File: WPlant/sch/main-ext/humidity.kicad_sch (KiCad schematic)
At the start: 20 parts, among them J11 HSensor, J12 HSensor, J13 HSensor, J14 HSensor, J15 HSensor, J16 HSensor, J17 HSensor, J18 WaterLevel, U12 CD74HCT4051M96, U13 CD74HCT4051M96, U14 SN74LVC1G14DBV

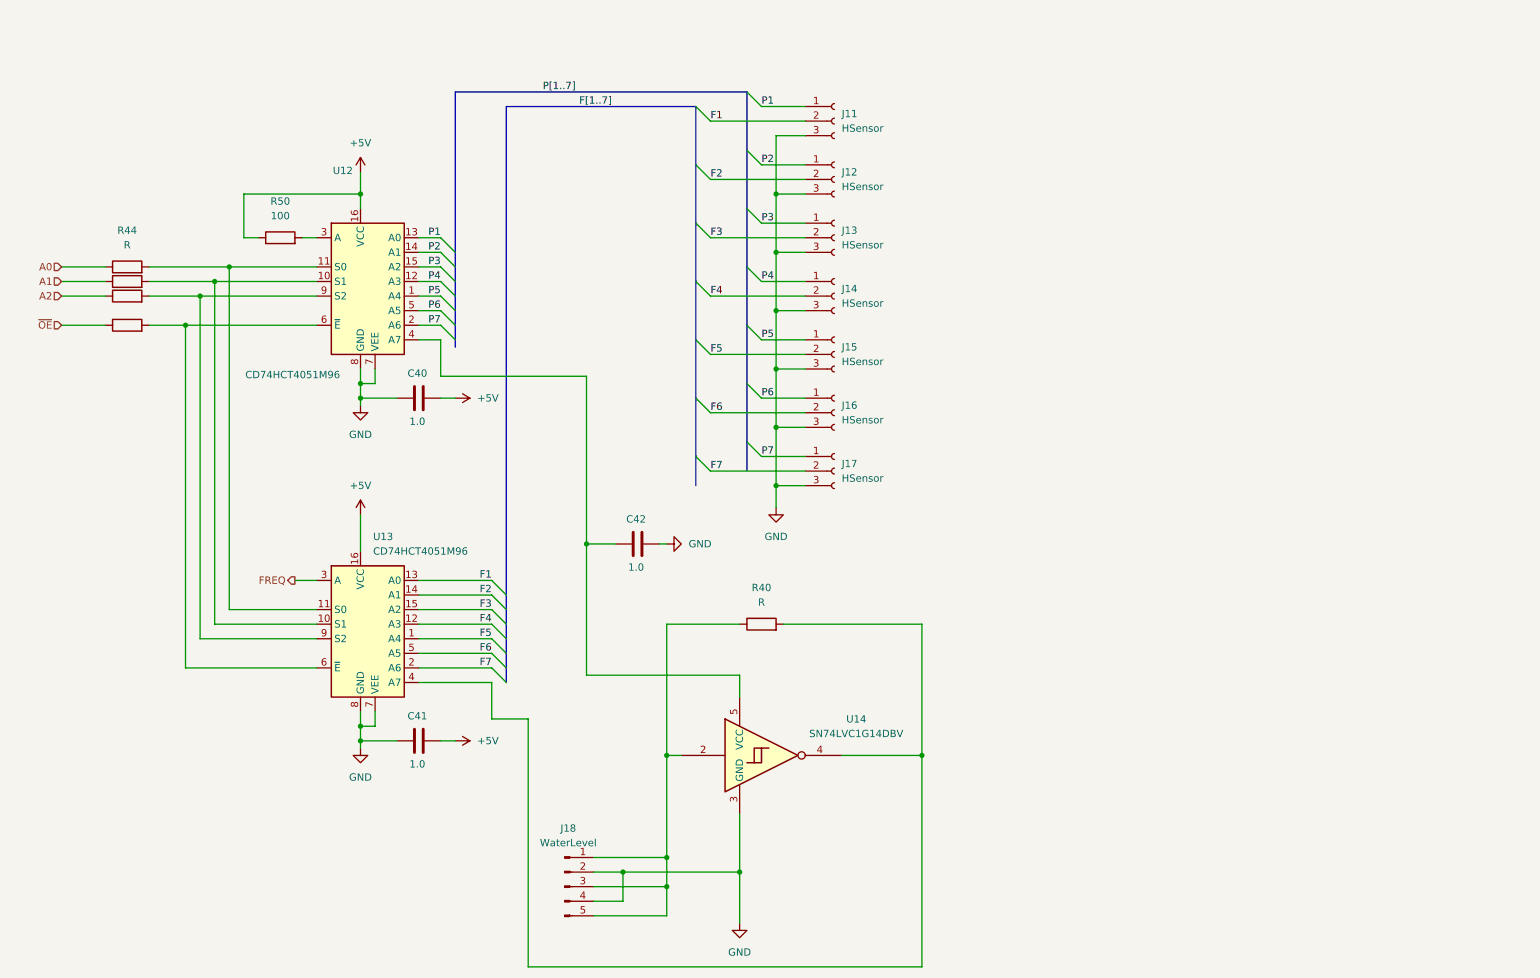
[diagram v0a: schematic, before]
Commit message: Route of WP project done
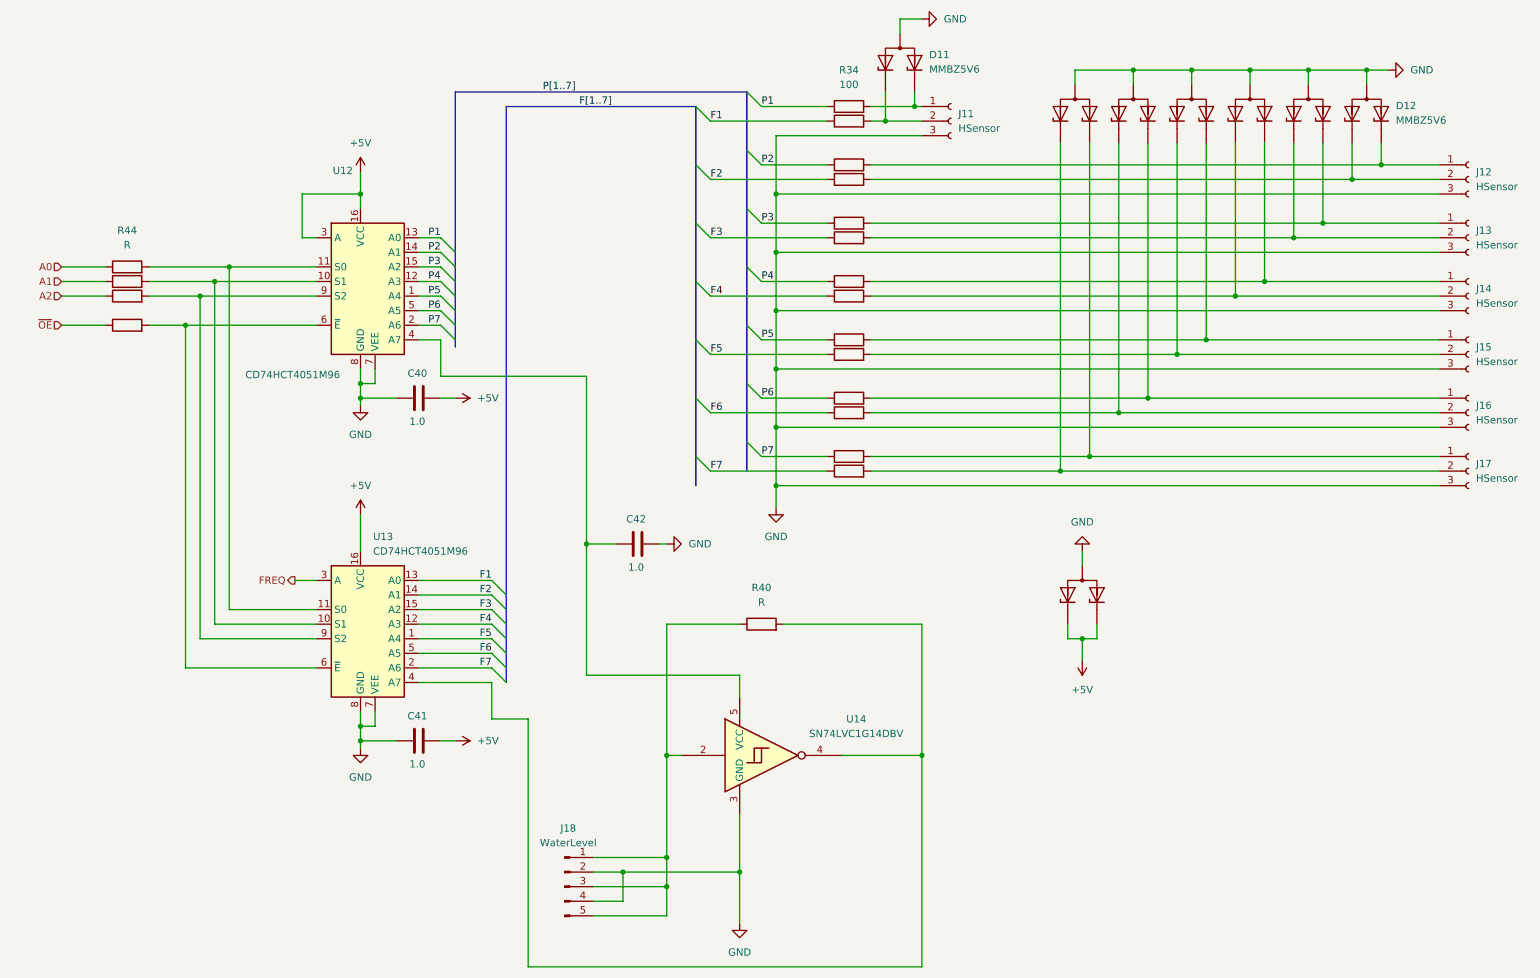
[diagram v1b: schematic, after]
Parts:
- added D11, D12, D13, D14, D15, D16, D17, D18: MMBZ5V6, Package_TO_SOT_SMD:SOT-23, symbol Diode:MMBZxx
- added R34, R51, R52, R53, R54, R55, R56, R57, R58, R59, R60, R61, R62: 100, Resistor_SMD:R_0603_1608Metric_Pad0.98x0.95mm_HandSolder, symbol Device:R
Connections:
- net +5V: now also U12.3 (A), D18.1 (K), D18.2 (K); no longer R50.1
- net F1: now also R50.1; no longer J11.2 (Pin_2)
- net F2: now also R52.1; no longer J12.2 (Pin_2)
- net F3: now also R54.1; no longer J13.2 (Pin_2)
- net F4: now also R56.1; no longer J14.2 (Pin_2)
- net F5: now also R58.1; no longer J15.2 (Pin_2)
- net F6: now also R60.1; no longer J16.2 (Pin_2)
- net F7: now also R62.1; no longer J17.2 (Pin_2)
- net GND: now also D11.3 (A), D12.3 (A), D13.3 (A), D14.3 (A), D15.3 (A), D16.3 (A), D17.3 (A), D18.3 (A)
- net P1: now also R34.1; no longer J11.1 (Pin_1)
- net P2: now also R51.1; no longer J12.1 (Pin_1)
- net P3: now also R53.1; no longer J13.1 (Pin_1)
- net P4: now also R55.1; no longer J14.1 (Pin_1)
- net P5: now also R57.1; no longer J15.1 (Pin_1)
- net P6: now also R59.1; no longer J16.1 (Pin_1)
- net P7: now also R61.1; no longer J17.1 (Pin_1)
- net at R50.2: now also J11.2 (Pin_2), D11.2 (K); no longer U12.3 (A)
- new net: D11.1 (K), J11.1 (Pin_1), R34.2
- new net: D13.1 (K), J13.1 (Pin_1), R53.2
- new net: D13.2 (K), J13.2 (Pin_2), R54.2
- new net: D12.1 (K), J12.1 (Pin_1), R51.2
- new net: D12.2 (K), J12.2 (Pin_2), R52.2
- new net: D16.1 (K), J16.1 (Pin_1), R59.2
- new net: D16.2 (K), J16.2 (Pin_2), R60.2
- new net: D14.1 (K), J14.1 (Pin_1), R55.2
- new net: D14.2 (K), J14.2 (Pin_2), R56.2
- new net: D17.1 (K), J17.1 (Pin_1), R61.2
- new net: D17.2 (K), J17.2 (Pin_2), R62.2
- new net: D15.1 (K), J15.1 (Pin_1), R57.2
- new net: D15.2 (K), J15.2 (Pin_2), R58.2
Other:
- moved on the sheet: J11, J12, J13, J14, J15, J16, J17

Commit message: Upate values in SCH of WP
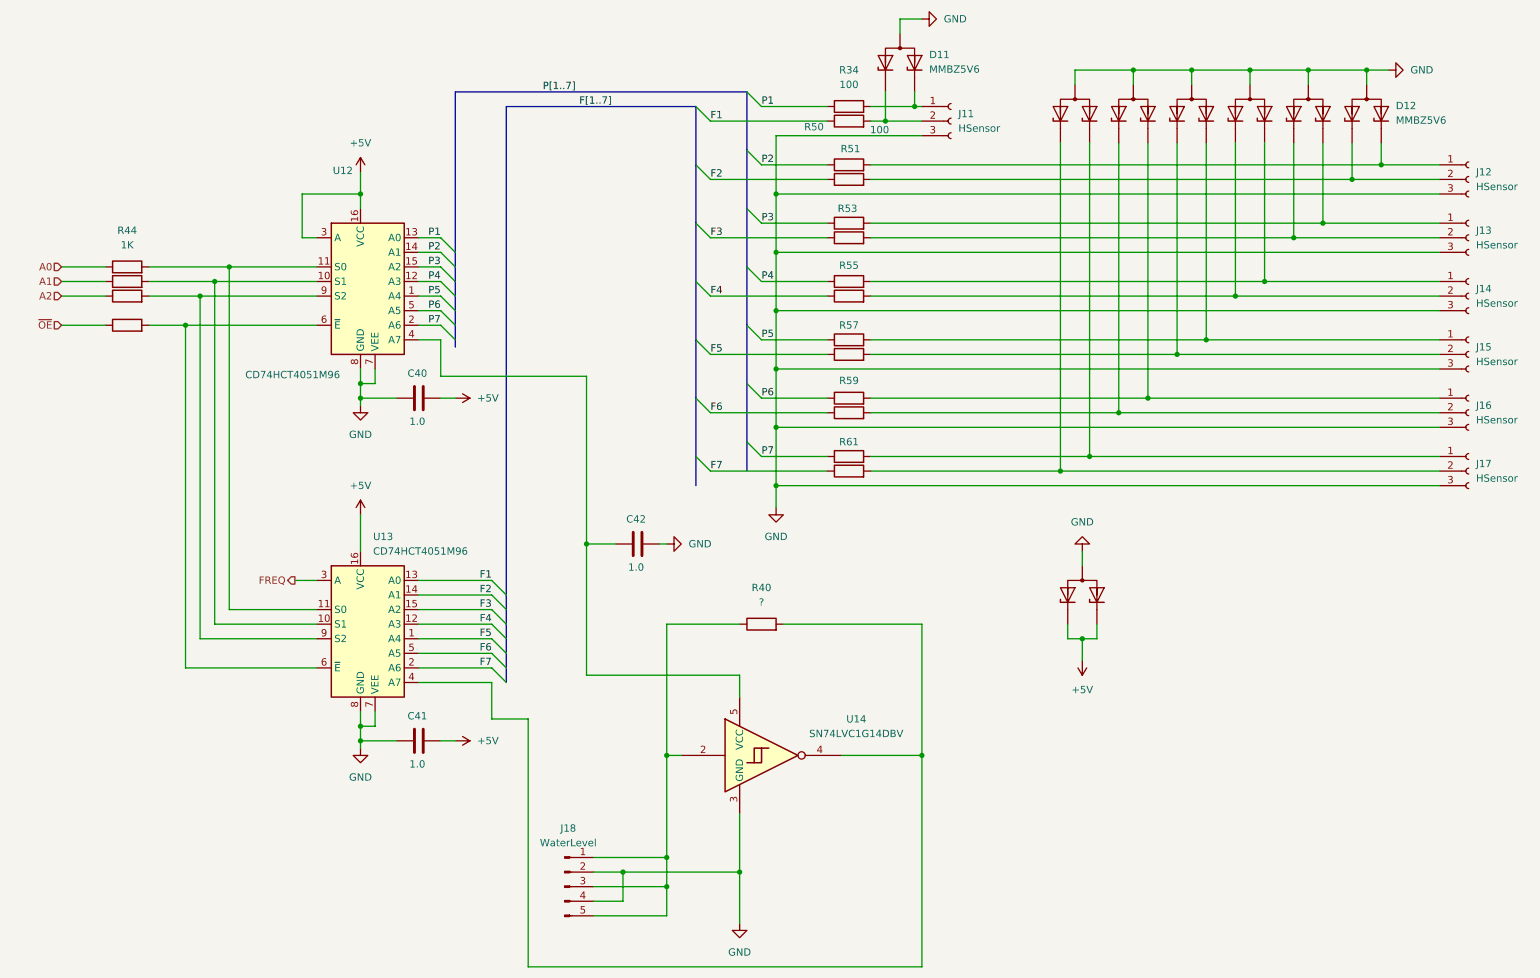
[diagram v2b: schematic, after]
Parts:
- R40: value R -> ?
- R44, R45, R46, R47: value R -> 1K
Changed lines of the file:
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@@
 		(on_board yes)
 		(dnp no)
-		(fields_autoplaced yes)
 		(property "Reference" "R50"
-			(at 162.56 27.94 90)
-			(effects
-				(font
-					(size 1.27 1.27)
-				)
-				(hide yes)
+			(at 156.464 35.306 90)
+			(effects
+				(font
+					(size 1.27 1.27)
+				)
 			)
 		)
 		(property "Value" "100"
-			(at 162.56 30.48 90)
-			(effects
-				(font
-					(size 1.27 1.27)
-				)
-				(hide yes)
+			(at 167.894 35.814 90)
+			(effects
+				(font
+					(size 1.27 1.27)
+				)
 			)
 		)
@@
 			)
 		)
-		(property "Value" "R"
+		(property "Value" "1K"
 			(at 36.83 60.96 90)
 			(effects
@@
 			)
 		)
-		(property "Value" "R"
+		(property "Value" "?"
 			(at 147.32 118.11 90)
 			(effects
@@
 		(on_board yes)
 		(dnp no)
-		(fields_autoplaced yes)
 		(property "Reference" "R53"
-			(at 162.56 45.72 90)
-			(effects
-				(font
-					(size 1.27 1.27)
-				)
-				(hide yes)
+			(at 162.306 49.53 90)
+			(effects
+				(font
+					(size 1.27 1.27)
+				)
 			)
 		)
@@
 			)
 		)
-		(property "Value" "R"
+		(property "Value" "1K"
 			(at 36.83 58.42 90)
 			(effects
@@
 		(on_board yes)
 		(dnp no)
-		(fields_autoplaced yes)
 		(property "Reference" "R55"
-			(at 162.56 55.88 90)
-			(effects
-				(font
-					(size 1.27 1.27)
-				)
-				(hide yes)
+			(at 162.56 59.436 90)
+			(effects
+				(font
+					(size 1.27 1.27)
+				)
 			)
 		)
@@
 		(on_board yes)
 		(dnp no)
-		(fields_autoplaced yes)
 		(property "Reference" "R61"
-			(at 162.56 86.36 90)
-			(effects
-				(font
-					(size 1.27 1.27)
-				)
-				(hide yes)
+			(at 162.56 90.17 90)
+			(effects
+				(font
+					(size 1.27 1.27)
+				)
 			)
 		)
@@
 		(on_board yes)
 		(dnp no)
-		(fields_autoplaced yes)
 		(property "Reference" "R51"
-			(at 162.56 35.56 90)
-			(effects
-				(font
-					(size 1.27 1.27)
-				)
-				(hide yes)
+			(at 162.814 39.116 90)
+			(effects
+				(font
+					(size 1.27 1.27)
+				)
 			)
 		)
@@
 			)
 		)
-		(property "Value" "R"
+		(property "Value" "1K"
 			(at 36.83 66.04 90)
 			(effects
@@
 		(on_board yes)
 		(dnp no)
-		(fields_autoplaced yes)
 		(property "Reference" "R59"
-			(at 162.56 76.2 90)
-			(effects
-				(font
-					(size 1.27 1.27)
-				)
-				(hide yes)
+			(at 162.56 79.502 90)
+			(effects
+				(font
+					(size 1.27 1.27)
+				)
 			)
 		)
@@
 		(on_board yes)
 		(dnp no)
-		(fields_autoplaced yes)
 		(property "Reference" "R57"
-			(at 162.56 66.04 90)
-			(effects
-				(font
-					(size 1.27 1.27)
-				)
-				(hide yes)
+			(at 162.56 69.85 90)
+			(effects
+				(font
+					(size 1.27 1.27)
+				)
 			)
 		)
@@
 			)
 		)
-		(property "Value" "R"
+		(property "Value" "1K"
 			(at 36.83 55.88 90)
 			(effects

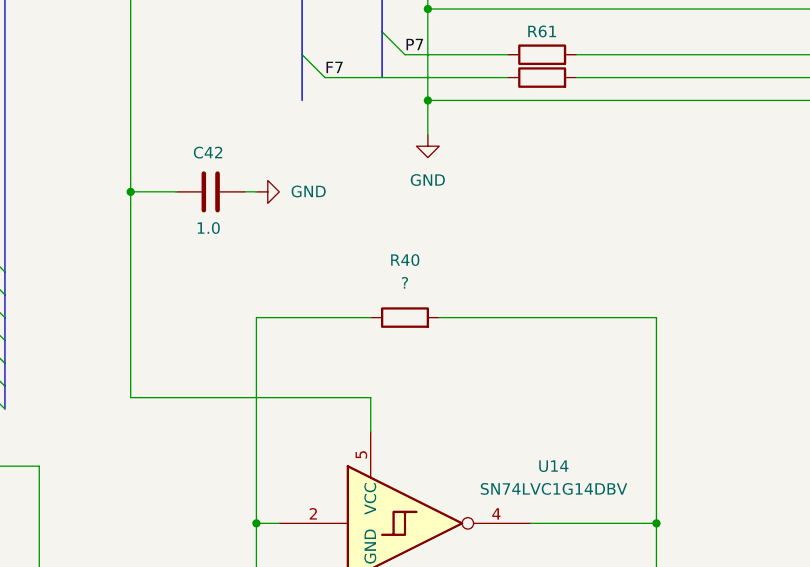
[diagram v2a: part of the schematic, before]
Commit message: Update WP Sch (sheets titles, replaced wires by bus, update components values)
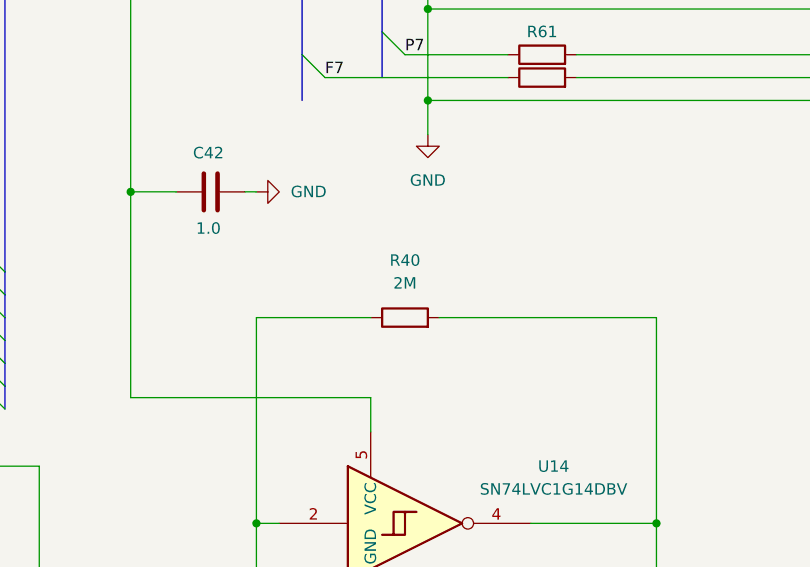
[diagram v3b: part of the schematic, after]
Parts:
- R40: value ? -> 2M
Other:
- title: Humidity sensors interface -> Humidity sensors interface  (WPMain Ext)
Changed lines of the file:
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@@
 	(paper "A4")
 	(title_block
-		(title "Humidity sensors interface")
+		(title "Humidity sensors interface  (WPMain Ext)")
+		(date "2026-02-05")
 		(company "RoboWay")
 	)
@@
 			)
 		)
-		(property "Value" "?"
+		(property "Value" "2M"
 			(at 147.32 118.11 90)
 			(effects
